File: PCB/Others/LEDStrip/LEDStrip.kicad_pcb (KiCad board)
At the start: 2 copper layers, 80 x 10 mm, 16 parts, among them J1 In, J2 Out

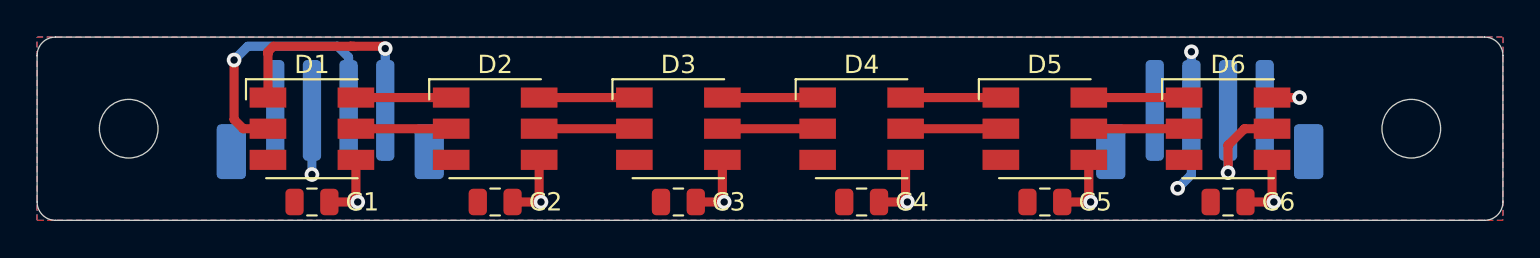
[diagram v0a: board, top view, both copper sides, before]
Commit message: Convert all KiCad to 6.0, clean up libraries, remove files that shouldn't be committed.
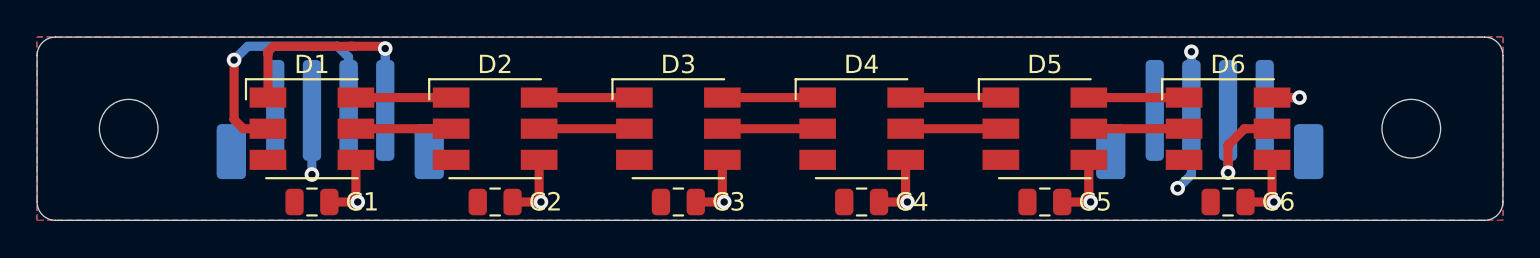
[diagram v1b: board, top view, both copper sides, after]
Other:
- net class Default removed
